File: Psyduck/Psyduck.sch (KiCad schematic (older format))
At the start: 19 parts, among them J1 ISP-6, J2 Conn_01x04_Male, J3 Conn_01x03_Male, U1 ATmega16M1-AU, U2 TJA1051T, U3 NCP1117-5V, Y1 Crystal

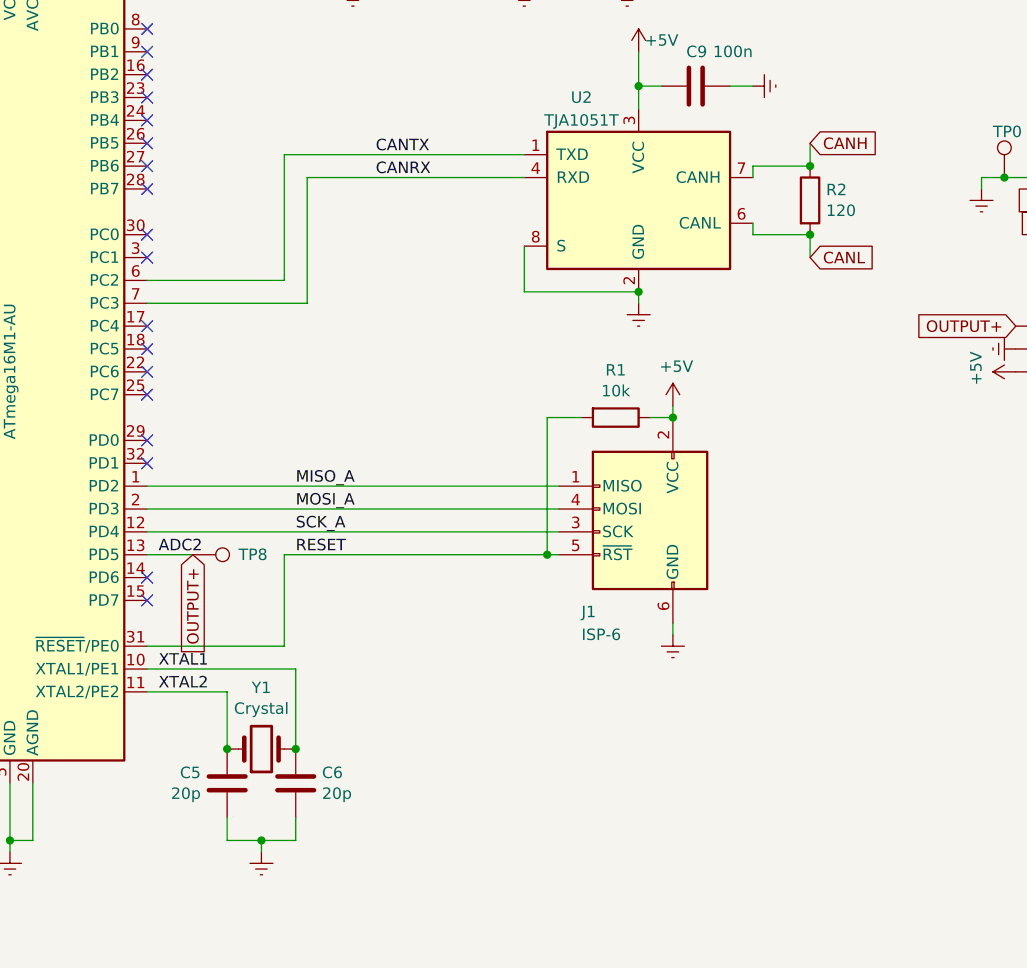
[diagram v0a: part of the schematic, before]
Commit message: Updated shematic and layout to accomodate changes from first round of testing
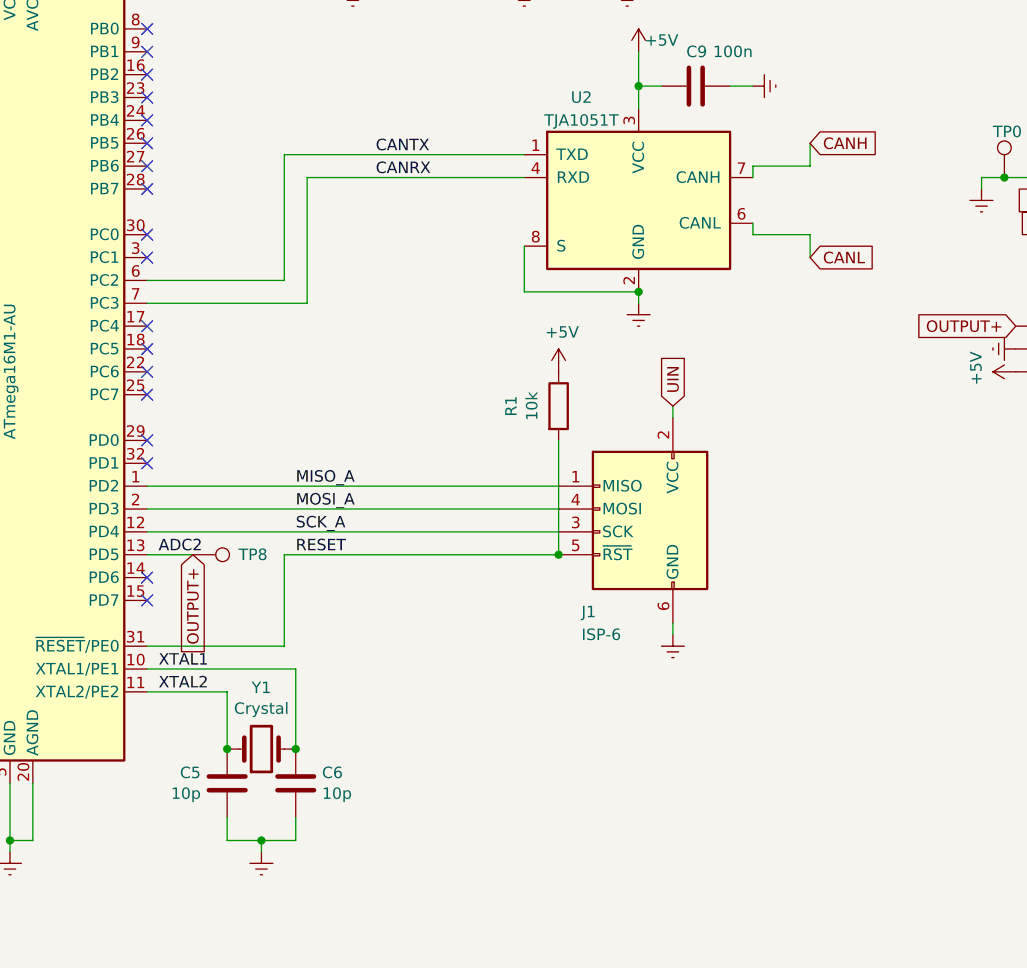
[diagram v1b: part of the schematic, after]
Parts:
- removed R2: 120, Resistor_SMD:R_0805_2012Metric_Pad1.15x1.40mm_HandSolder, symbol Device:R
- C5, C6: value 20p -> 10p
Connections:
- net +5V: no longer J1.2 (VCC)
- net UIN: now also J1.2 (VCC)
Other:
- moved on the sheet: R1
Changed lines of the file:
@@
 L Device:R R1
 U 1 1 5E206CE8
-P 3950 3250
-F 0 "R1" V 3743 3250 50  0000 C CNN
-F 1 "10k" V 3834 3250 50  0000 C CNN
-F 2 "Resistor_SMD:R_0805_2012Metric_Pad1.15x1.40mm_HandSolder" V 3880 3250 50  0001 C CNN
-F 3 "~" H 3950 3250 50  0001 C CNN
-	1    3950 3250
-	0    1    1    0
+P 3700 3200
+F 0 "R1" V 3493 3200 50  0000 C CNN
+F 1 "10k" V 3584 3200 50  0000 C CNN
+F 2 "Resistor_SMD:R_0805_2012Metric_Pad1.15x1.40mm_HandSolder" V 3630 3200 50  0001 C CNN
+F 3 "~" H 3700 3200 50  0001 C CNN
+	1    3700 3200
+	1    0    0    -1
 $EndComp
 $Comp
@@
 	1900 3550 3700 3550
 Wire Wire Line
-	3650 3250 3650 3850
-Wire Wire Line
 	1900 4350 2550 4350
 Wire Wire Line
@@
 Wire Wire Line
 	2500 4250 2500 3850
-Wire Wire Line
-	3650 3250 3800 3250
-Connection ~ 3650 3850
-Wire Wire Line
-	3650 3850 3700 3850
 Wire Wire Line
 	2500 2100 2500 2650
@@
 L power:+5V #PWR0111
 U 1 1 5E3265FD
-P 4200 3200
-F 0 "#PWR0111" H 4200 3050 50  0001 C CNN
-F 1 "+5V" H 4215 3373 50  0000 C CNN
-F 2 "" H 4200 3200 50  0001 C CNN
-F 3 "" H 4200 3200 50  0001 C CNN
-	1    4200 3200
-	1    0    0    -1
-$EndComp
-Wire Wire Line
-	4100 3250 4200 3250
+P 3700 3050
+F 0 "#PWR0111" H 3700 2900 50  0001 C CNN
+F 1 "+5V" H 3715 3223 50  0000 C CNN
+F 2 "" H 3700 3050 50  0001 C CNN
+F 3 "" H 3700 3050 50  0001 C CNN
+	1    3700 3050
+	1    0    0    -1
+$EndComp
 Wire Wire Line
 	4200 3200 4200 3250
-Connection ~ 4200 3250
 Wire Wire Line
 	2800 1250 2800 1350
@@
 Wire Wire Line
 	3800 950  4000 950
-Wire Wire Line
-	2500 3850 3650 3850
 $Comp
 L power:Earth #PWR0114
@@
 P 2550 4850
 F 0 "C6" H 2665 4896 50  0000 L CNN
-F 1 "20p" H 2665 4805 50  0000 L CNN
+F 1 "10p" H 2665 4805 50  0000 L CNN
 F 2 "Capacitor_SMD:C_0805_2012Metric_Pad1.15x1.40mm_HandSolder" H 2588 4700 50  0001 C CNN
 F 3 "~" H 2550 4850 50  0001 C CNN
@@
 P 2250 4850
 F 0 "C5" H 2365 4896 50  0000 L CNN
-F 1 "20p" H 2365 4805 50  0000 L CNN
+F 1 "10p" H 2365 4805 50  0000 L CNN
 F 2 "Capacitor_SMD:C_0805_2012Metric_Pad1.15x1.40mm_HandSolder" H 2288 4700 50  0001 C CNN
 F 3 "~" H 2250 4850 50  0001 C CNN
@@
 Text GLabel 6000 2400 0    50   Input ~ 0
 CANL
-$Comp
-L Device:R R2
-U 1 1 5E2D33A5
-P 4800 2300
-F 0 "R2" H 4870 2346 50  0000 L CNN
-F 1 "120" H 4870 2255 50  0000 L CNN
-F 2 "Resistor_SMD:R_0805_2012Metric_Pad1.15x1.40mm_HandSolder" V 4730 2300 50  0001 C CNN
-F 3 "~" H 4800 2300 50  0001 C CNN
-	1    4800 2300
-	1    0    0    -1
-$EndComp
 Wire Wire Line
 	4550 2400 4550 2450
@@
 Wire Wire Line
 	4800 2550 4800 2450
-Connection ~ 4800 2450
 Wire Wire Line
 	4550 2200 4550 2150
@@
 Wire Wire Line
 	4800 2050 4800 2150
-Connection ~ 4800 2150
 Wire Wire Line
 	4050 1650 4050 1800
@@
 	1    0    0    -1
 $EndComp
+Wire Wire Line
+	2500 3850 3700 3850
+Connection ~ 3700 3850
+Wire Wire Line
+	3700 3350 3700 3850
+Text GLabel 4200 3200 1    50   Input ~ 0
+UIN
 $EndSCHEMATC
